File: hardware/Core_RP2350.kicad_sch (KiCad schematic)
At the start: 70 parts, among them U1 RP2350B-QFN80, U2 LM4040A30IDBZR, U3 W25Q128JVS, U4 W25Q128JVS, U5 W25Q128JVS

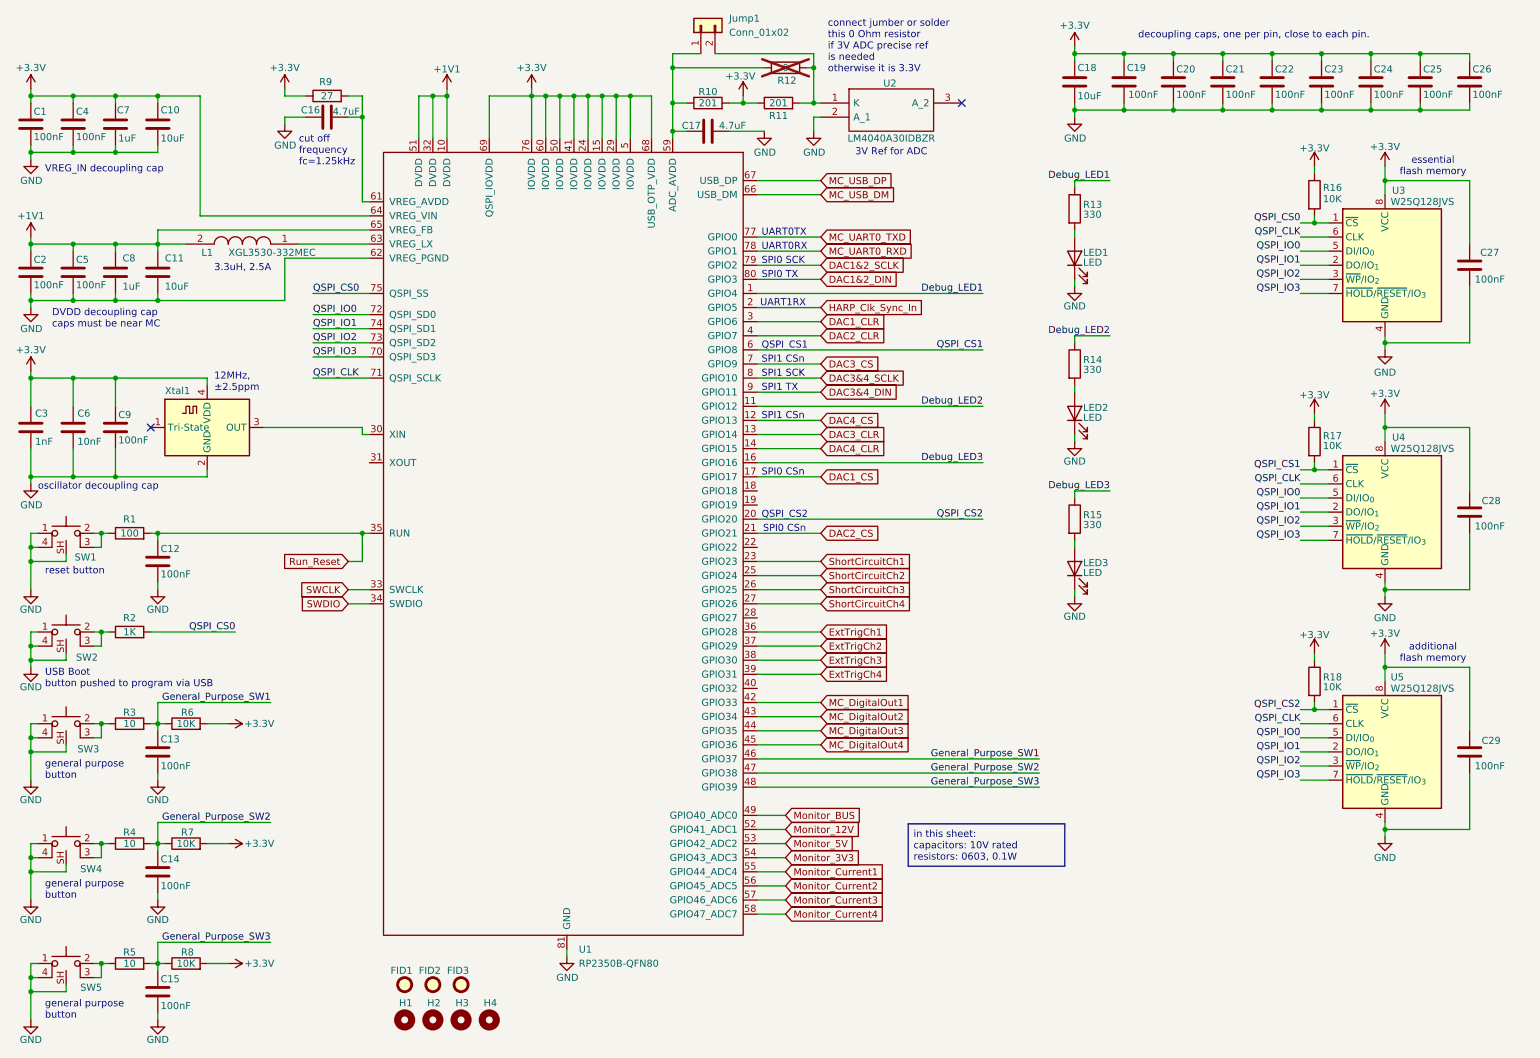
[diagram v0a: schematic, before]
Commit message: BOM for all capacitors and resistors is added correctly to the schematic
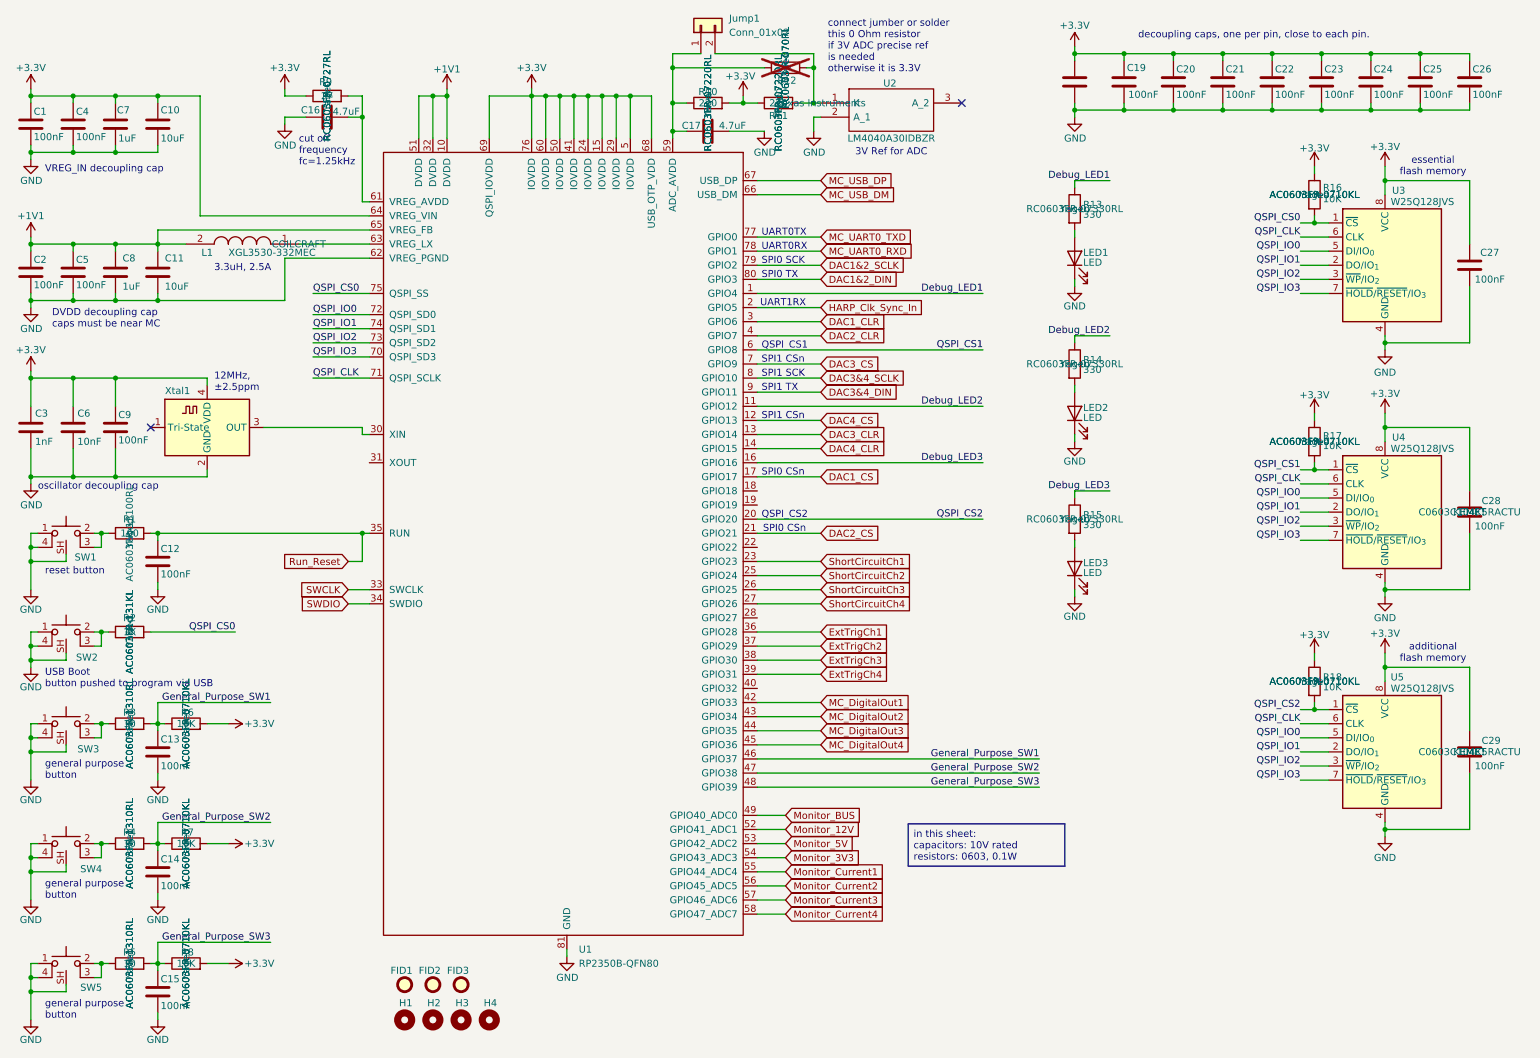
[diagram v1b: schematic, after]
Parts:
- C1, C12, C13, C14, C15, C19, C2, C20, C21, C22, C23, C24, C25, C26, C27, C28, C29, C4, C5, C9: Link https://www.digikey.com/en/products/detail/walsin-technolog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 -> https://www.digikey.com/en/products/detail/kemet/C0603C104K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; MPN (none) -> C0603C104K5RACTU; Manufacturer Walson Technology Corporation -> KEMET; Manufacturer Number 0402B104K160CT -> (none); Manufacturer_Name (none) -> KEMET; Manufacturer_Part_Number (none) -> C0603C104K5RACTU; Rated Voltage 16V -> 50V
- C10, C11, C18: Link https://www.digikey.com/en/products/detail/murata-electronics/GRM21BZ71E106KE15L/13904911 -> https://www.digikey.com/en/products/detail/murata-electronics/GRM188R61E106KA73D/9867922; MPN (none) -> GRM188R61E106KA73D; Manufacturer Number GRM21BZ71E106KE15L -> (none); Manufacturer_Name (none) -> Murata Electronics; Manufacturer_Part_Number (none) -> GRM188R61E106KA73D; Tolerance (none) -> 10%
- C16, C17: Link https://www.digikey.com/en/products/detail/murata-electroni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 -> https://www.digikey.com/en/products/detail/tdk-corporation/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; MPN (none) -> C1608X5R1V475K080AC; Manufacturer Murata Electronics -> TDK Corporation; Manufacturer Number GRM21BZ71E106KE15L -> (none); Manufacturer_Name (none) -> TDK Corporation; Manufacturer_Part_Number (none) -> C1608X5R1V475K080AC; Rated Voltage 25V -> 35V; Tolerance (none) -> 10%
- C3: Link https://www.digikey.com/en/products/detail/yageo/CC0402KPX7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 -> https://www.digikey.com/en/products/detail/kemet/C0603C102K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; MPN (none) -> C0603C102K5RACTU; Manufacturer Yageo -> KEMET; Manufacturer Number CC0402KPX7R8BB103 -> (none); Manufacturer_Name (none) -> KEMET; Manufacturer_Part_Number (none) -> C0603C102K5RACTU; Rated Voltage 25V -> 50V
- C6: Link https://www.digikey.com/en/products/detail/yageo/CC0402KPX7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 -> https://www.digikey.com/en/products/detail/kemet/C0603C103K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; MPN (none) -> C0603C103K5RACTU; Manufacturer Yageo -> KEMET; Manufacturer Number CC0402KPX7R8BB103 -> (none); Manufacturer_Name (none) -> KEMET; Manufacturer_Part_Number (none) -> C0603C103K5RACTU; Rated Voltage 25V -> 50V
- C7, C8: Link https://www.digikey.com/en/products/detail/murata-electroni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 -> https://www.digikey.com/en/products/detail/tdk-corporation/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; MPN (none) -> C1608X7R1H105K080AB; Manufacturer Murata Electronics -> TDK Corporation; Manufacturer Number GRM155R6YA105KE11J -> (none); Manufacturer_Name (none) -> TDK Corporation; Manufacturer_Part_Number (none) -> C1608X7R1H105K080AB; Rated Voltage 35V -> 50V; Tolerance (none) -> 10%
- L1: Manufacturer (none) -> COILCRAFT
- R1: Link https://www.digikey.com/en/products/detail/yageo/RT0402BRD0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 -> https://www.digikey.com/en/products/detail/yageo/AC0603FR-1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; MPN (none) -> AC0603FR-13100RL; Manufacturer_Name (none) -> Yageo; Manufacturer_Part_Number (none) -> AC0603FR-13100RL
- R10, R11: value 201 -> 220; Link https://www.digikey.com/en/products/detail/yageo/RT0402BRD0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 -> https://www.digikey.com/en/products/detail/yageo/RC0603FR-0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; MPN (none) -> RC0603FR-07220RL; Manufacturer_Name (none) -> Yageo; Manufacturer_Part_Number (none) -> RC0603FR-07220RL
- R12: Link https://www.digikey.com/en/products/detail/yageo/RT0402BRD0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 -> https://www.digikey.com/en/products/detail/yageo/RC0603JR-0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; MPN (none) -> RC0603JR-070RL; Manufacturer_Name (none) -> Yageo; Manufacturer_Part_Number (none) -> RC0603JR-070RL; Tolerance 1% -> (none)
- R13, R14, R15: Link https://www.digikey.com/en/products/detail/yageo/RC0402FR-0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 -> https://www.digikey.com/en/products/detail/yageo/RC0603FR-0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; MPN (none) -> RC0603FR-07330RL; Manufacturer_Name (none) -> Yageo; Manufacturer_Part_Number (none) -> RC0603FR-07330RL
- R16, R17, R18: Link https://www.digikey.com/en/products/detail/koa-speer-electr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 -> https://www.digikey.com/en/products/detail/yageo/AC0603FR-0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; MPN (none) -> AC0603FR-0710KL; Manufacturer KOA Speer Electronics, Inc. -> Yageo; Manufacturer_Name (none) -> Yageo; Manufacturer_Part_Number (none) -> AC0603FR-0710KL; Tolerance (none) -> 1%
- R2: Link https://www.digikey.com/en/products/detail/yageo/RT0402BRD0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 -> https://www.digikey.com/en/products/detail/yageo/AC0603FR-1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; MPN (none) -> AC0603FR-131KL; Manufacturer_Name (none) -> Yageo; Manufacturer_Part_Number (none) -> AC0603FR-131KL
- R3, R4, R5: Link https://www.digikey.com/en/products/detail/yageo/RT0402BRD0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 -> https://www.digikey.com/en/products/detail/yageo/AC0603FR-1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; MPN (none) -> AC0603FR-1310RL; Manufacturer_Name (none) -> Yageo; Manufacturer_Part_Number (none) -> AC0603FR-1310RL
- R6, R7, R8: Link https://www.digikey.com/en/products/detail/yageo/RT0402BRD0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 -> https://www.digikey.com/en/products/detail/yageo/AC0603FR-0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; MPN (none) -> AC0603FR-0710KL; Manufacturer_Name (none) -> Yageo; Manufacturer_Part_Number (none) -> AC0603FR-0710KL
- R9: Link https://www.digikey.com/en/products/detail/yageo/RT0402BRD0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 -> https://www.digikey.com/en/products/detail/yageo/RC0603FR-0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; MPN (none) -> RC0603FR-0727RL; Manufacturer_Name (none) -> Yageo; Manufacturer_Part_Number (none) -> RC0603FR-0727RL
- U2: Manufacturer (none) -> Texas Instruments

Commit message: Not necessary text is hidden + BOM on schematic
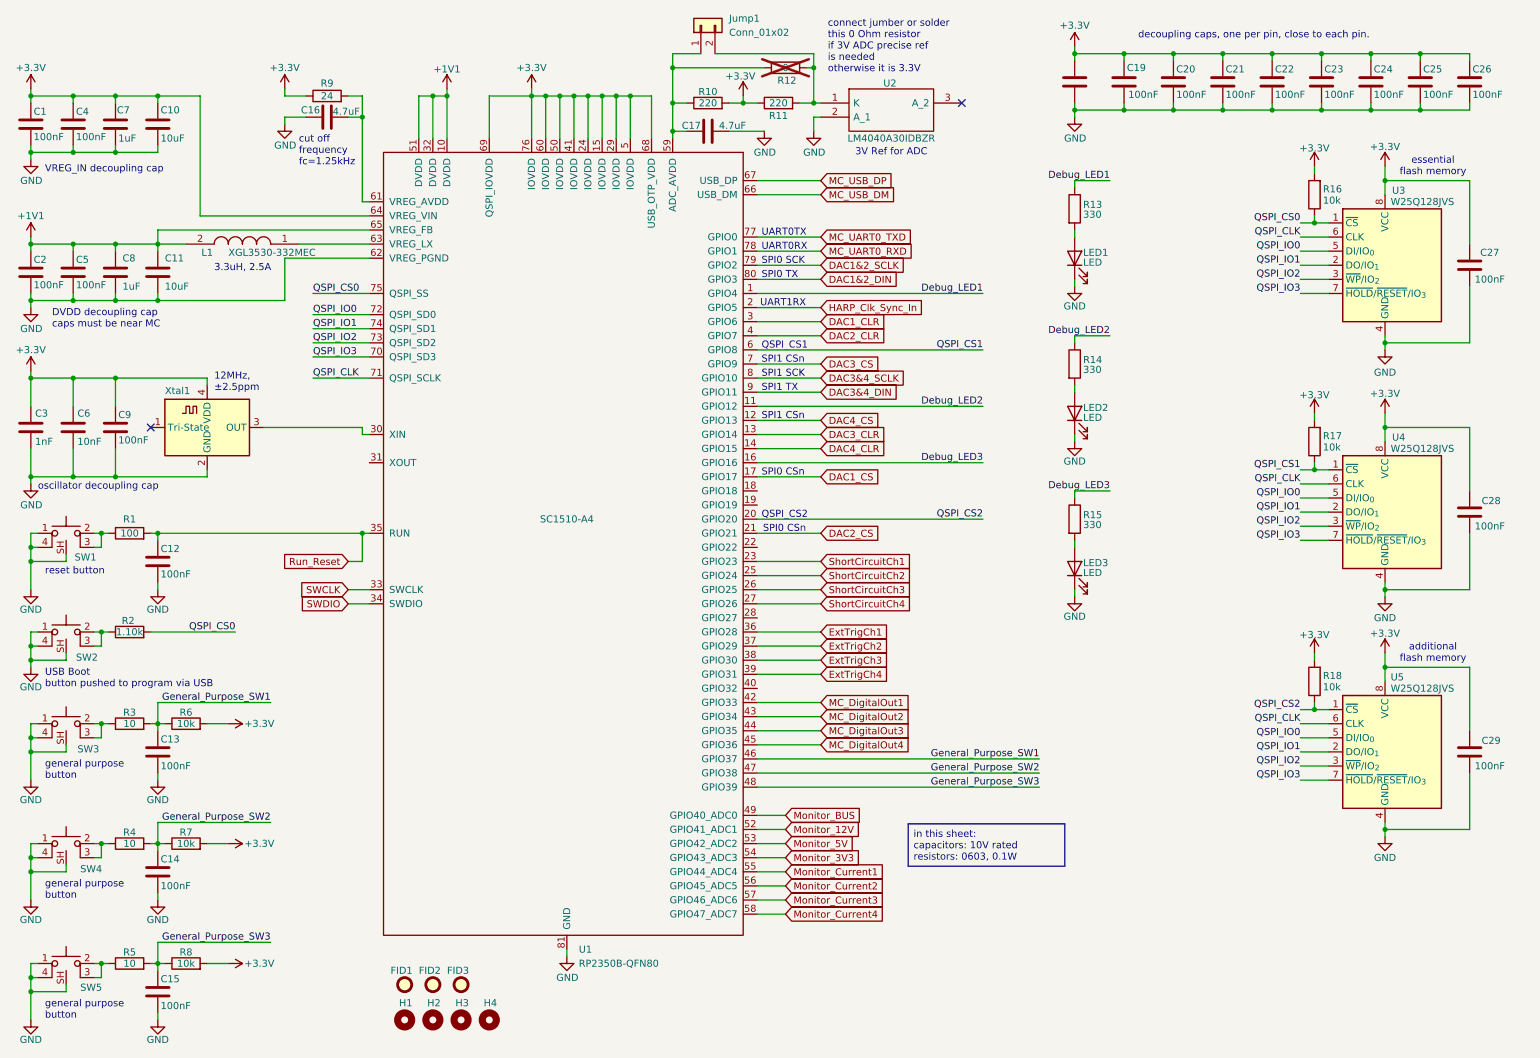
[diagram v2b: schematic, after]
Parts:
- C1, C10, C11, C12, C13, C14, C15, C16, C17, C18, C19, C2, C20, C21, C22, C23, C24, C25, C26, C27, C28, C29, C3, C4, C5, C6, C9: Temperature Coefficient X7R -> (none)
- C7, C8: Temperature Coefficient X5R -> (none)
- L1: MPN (none) -> XGL3530-332MEC
- LED1, LED2, LED3: Manufacturer_Part_Number (none) -> XZCDGK53W-1VF
- R16, R17, R18: value 10K -> 10k; Link https://www.digikey.com/en/products/detail/yageo/AC0603FR-0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 -> https://www.digikey.com/en/products/detail/yageo/RT0603BRD0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; MPN AC0603FR-0710KL -> RT0603BRD0710KL; Manufacturer Number SG73P1EWTTP1002F -> RT0402BRD071KL; Manufacturer_Part_Number AC0603FR-0710KL -> RT0603BRD0710KL; Tolerance 1% -> 0.1%
- R2: value 1K -> 1.10k; Link https://www.digikey.com/en/products/detail/yageo/AC0603FR-1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 -> https://www.digikey.com/en/products/detail/yageo/RT0603BRD0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; MPN AC0603FR-131KL -> RT0603BRD071K1L; Manufacturer Number RT0402BRD071KL -> RC0402FR-07680RL; Manufacturer_Part_Number AC0603FR-131KL -> RT0603BRD071K1L; Tolerance 1% -> 0.1%
- R6, R7, R8: value 10K -> 10k; Link https://www.digikey.com/en/products/detail/yageo/AC0603FR-0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 -> https://www.digikey.com/en/products/detail/yageo/RT0603BRD0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; MPN AC0603FR-0710KL -> RT0603BRD0710KL; Manufacturer_Part_Number AC0603FR-0710KL -> RT0603BRD0710KL; Tolerance 1% -> 0.1%
- R9: value 27 -> 24; Link https://www.digikey.com/en/products/detail/yageo/RC0603FR-0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 -> https://www.digikey.com/en/products/detail/yageo/AC0603FR-0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; MPN RC0603FR-0727RL -> AC0603FR-0724RL; Manufacturer Number RT0402BRD071KL -> AC0402FR-0724RL; Manufacturer_Part_Number RC0603FR-0727RL -> AC0603FR-0724RL
- SW1, SW2, SW3, SW4, SW5: Manufacturer_Part_Number (none) -> 435451019820
- U1: Manufacturer_Part_Number (none) -> SC1510-A4
- U2: MPN (none) -> LM4040A30IDBZR
- Xtal1: Manufacturer_Part_Number (none) -> ECS-TXO-2016-33-120-TR
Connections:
- net +3.3V: now also R16.2, R17.2, R18.2; no longer R16.1, R17.1, R18.1
- net QSPI_CS0: now also R16.1; no longer R16.2
- net QSPI_CS1: now also R17.1; no longer R17.2
- net QSPI_CS2: now also R18.1; no longer R18.2

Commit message: BOM cont.
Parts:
- FID1, FID2, FID3: MPN (none) -> n/a; Manufacturer_Name (none) -> n/a; Manufacturer_Part_Number (none) -> n/a
- H1, H2, H3, H4: Link (none) -> n/a; MPN (none) -> n/a; Manufacturer (none) -> n/a; Manufacturer_Name (none) -> n/a; Manufacturer_Part_Number (none) -> n/a
- Jump1: Link (none) -> https://www.digikey.com/en/products/detail/harwin-inc/M20-9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; MPN (none) -> M20-9990246; Manufacturer (none) -> Harwin Inc.; Manufacturer_Name (none) -> Harwin Inc.; Manufacturer_Part_Number (none) -> M20-9990246

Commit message: TVS16,TVS17,TVS18,TVS19 parts have been changed from ESDSB12VLB-TP to PESD12VL1BSLAZ
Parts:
- U2: footprint SOT95P237X112-3N -> harp.device.quad.dac.kicad:SOT95P237X112-3N
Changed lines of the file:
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@@
 			)
 		)
-		(property "Footprint" "SOT95P237X112-3N"
+		(property "Footprint" "harp.device.quad.dac.kicad:SOT95P237X112-3N"
 			(at 182.88 25.4 0)
 			(effects

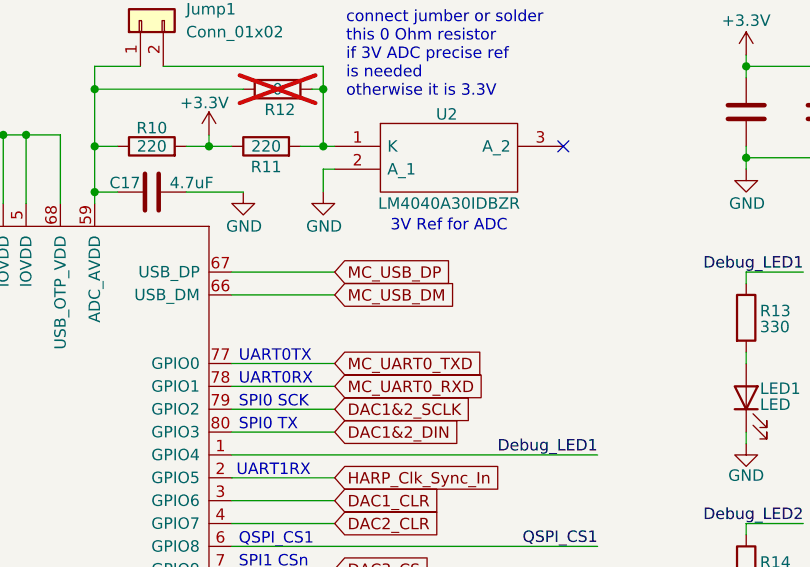
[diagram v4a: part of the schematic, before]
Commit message: Rename Some nets
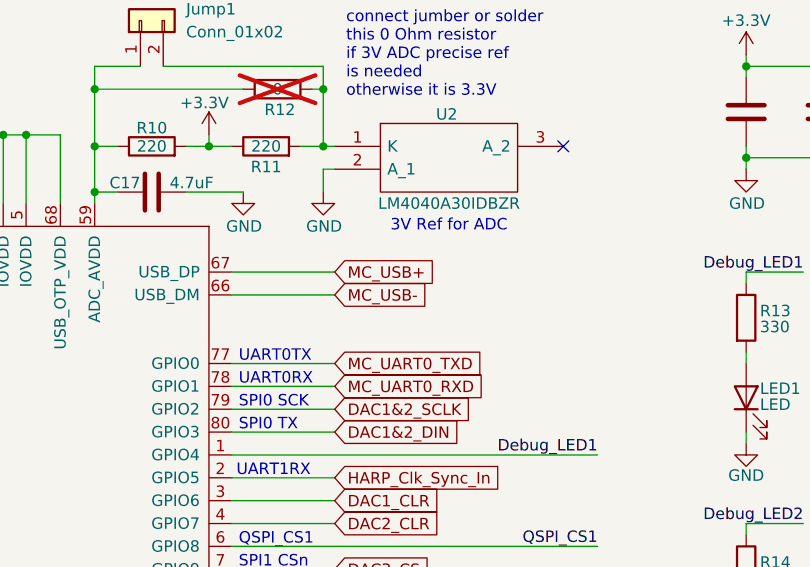
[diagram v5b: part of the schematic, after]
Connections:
- net MC_USB_DM renamed MC_USB-
- net MC_USB_DP renamed MC_USB+
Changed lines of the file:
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@@
 		)
 	)
-	(global_label "MC_USB_DM"
+	(global_label "MC_USB-"
 		(shape input)
 		(at 161.29 44.45 0)
@@
 		)
 		(property "Intersheetrefs" "${INTERSHEET_REFS}"
-			(at 175.4632 44.45 0)
+			(at 173.3466 44.45 0)
 			(effects
 				(font
@@
 		)
 	)
-	(global_label "MC_USB_DP"
+	(global_label "MC_USB+"
 		(shape input)
 		(at 161.29 41.91 0)
@@
 		)
 		(property "Intersheetrefs" "${INTERSHEET_REFS}"
-			(at 175.2818 41.91 0)
-			(effects
-				(font
+			(at 173.3466 41.91 0)
+			(effects
+				(font

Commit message: Continue BOM + enhance BOM + enhance schematic
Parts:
- C16, C17, C7, C8: Manufacturer TDK Corporation -> TDK; Manufacturer_Name TDK Corporation -> TDK
- Jump1: Manufacturer Harwin Inc. -> Harwin; Manufacturer_Name Harwin Inc. -> Harwin
- L1: Link (none) -> https://www.digikey.com/en/products/detail/coilcraft/XGL353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
- LED1, LED2, LED3: Manufacturer_Name (none) -> SunLED
- SW1, SW2, SW3, SW4, SW5: value ~ -> SPST-NO; Link (none) -> https://www.digikey.com/en/products/detail/w%C3%BCrth-elekt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; Manufacturer (none) -> Würth Elektronik; Manufacturer_Name (none) -> Würth Elektronik
- U1: Link (none) -> https://www.digikey.com/en/products/detail/raspberry-pi/SC1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; Manufacturer (none) -> Raspberry Pi; Manufacturer_Name (none) -> Raspberry Pi
- U2: Link (none) -> https://www.digikey.com/en/products/detail/texas-instrument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
- U3, U4, U5: Link (none) -> https://www.digikey.com/en/products/detail/winbond-electron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; MPN (none) -> W25Q128JVSIQ TR; Manufacturer (none) -> Winbond Electronics; Manufacturer_Name (none) -> Winbond Electronics; Manufacturer_Part_Number (none) -> W25Q128JVSIQ TR
- Xtal1: Manufacturer ECS Inc. -> ECS; Manufacturer_Name (none) -> ECS
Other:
- note added: "Red"
